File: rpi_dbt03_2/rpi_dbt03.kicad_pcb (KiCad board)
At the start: 2 copper layers, 64 x 56 mm, 33 parts, among them J2 Conn_02x03_Odd_Even, Q1 BC546, U1 ATmega8L-8PU, U2 SFH617A-1, U3 SFH617A-1, U4 SFH617A-1, Y1 8MHz

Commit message: Found a hardware Bug. Pin 18 of the ATMega8 needs to connected to Pin 24 of the Raspberry PI. This will mean that a new layout is needed, however so far you can patch it by adding one bodge wire.
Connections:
- RP1 pad 24: Net-(RP1-Pad24) -> /SPI_CS
- U1 pad 16: Net-(U1-Pad16) -> /SPI_CS
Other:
- board text added: "Warning one unconnected wire in this revision!"

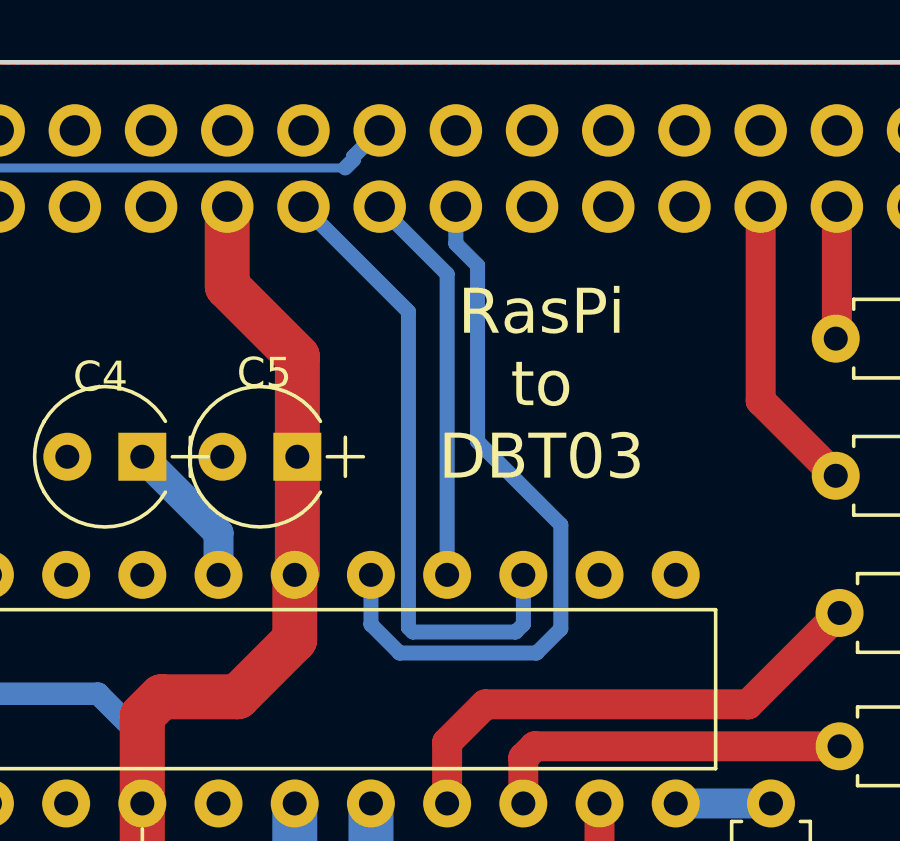
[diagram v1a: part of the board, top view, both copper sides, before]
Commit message: Added SPI_CE line and swapped incorrectly named _SD0 and _S0 netw
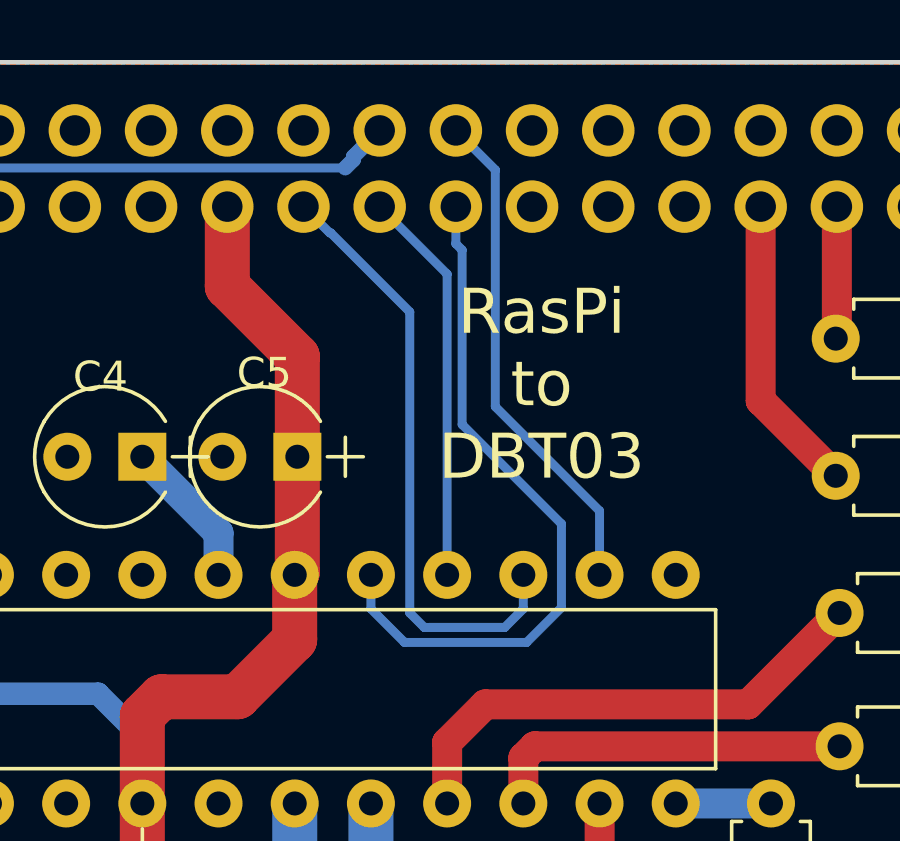
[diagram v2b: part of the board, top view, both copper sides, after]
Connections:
- R3 pad 2: /_S0 -> /_SD0
- R4 pad 2: /_SD0 -> /_S0
- U1 pad 2: /_SD0 -> /_S0
- U1 pad 3: /_S0 -> /_SD0
- U2 pad 4: /_SD0 -> /_S0
- U3 pad 4: /_S0 -> /_SD0
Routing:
- net /SPI_CS: track 0.00 -> 16.8 mm
- net /_SD0: track 33.2 -> 25.8 mm
- net /_S0: track 25.8 -> 33.2 mm
- net /MOSI: track 21.1 -> 22.9 mm
- net /SCK: track 24.2 -> 23.3 mm
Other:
- board text removed: "Warning one unconnected wire in this revision!"

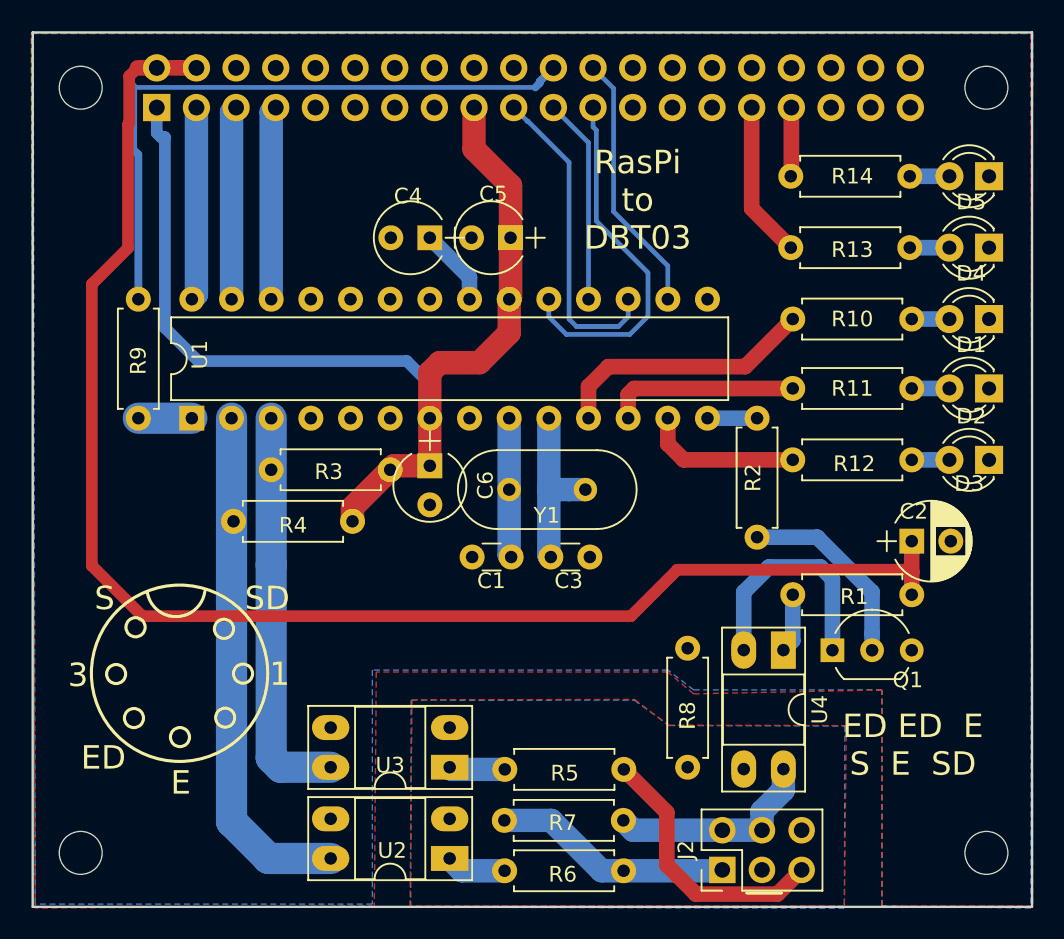
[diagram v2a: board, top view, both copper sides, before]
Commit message: Minor change, I think 2 network names have been swapped
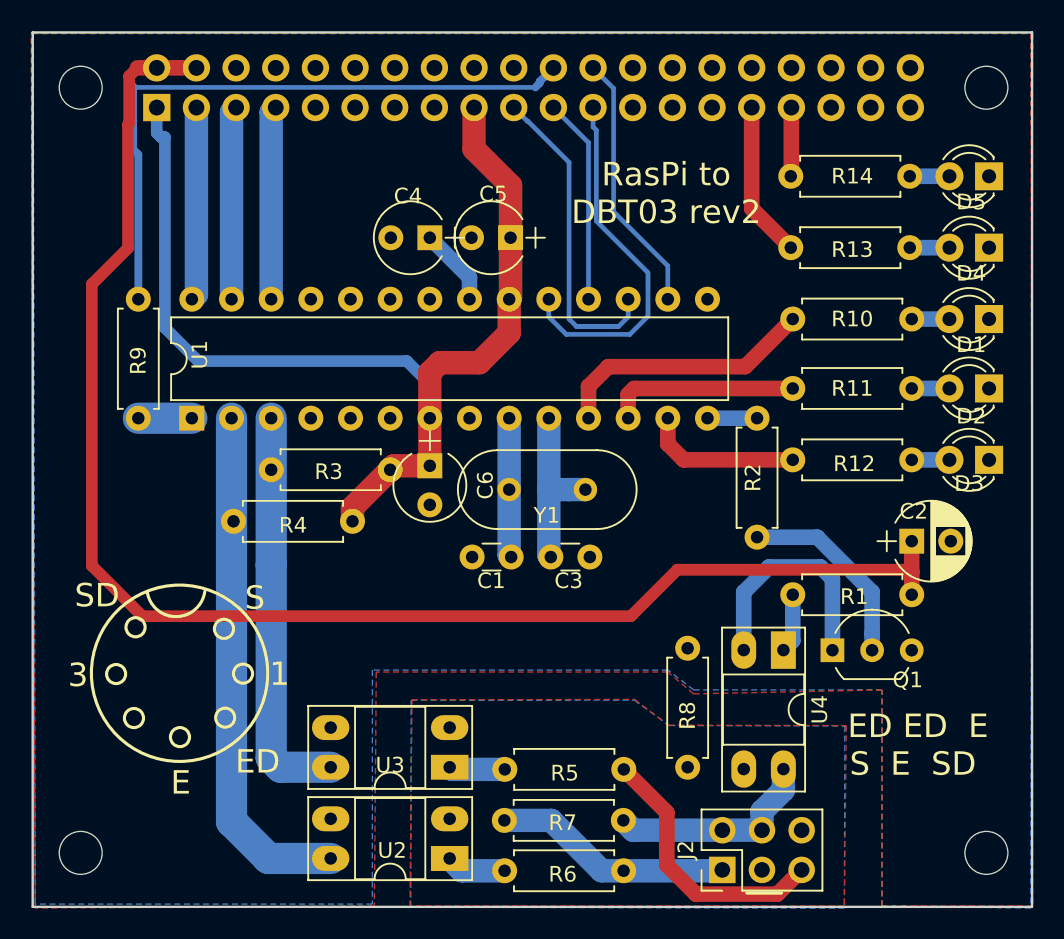
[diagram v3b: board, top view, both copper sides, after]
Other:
- board text added: "RasPi to DBT03 rev2"
- board text removed: "RasPi to DBT03"
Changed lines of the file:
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@@
   )
   (setup
-    (last_trace_width 0.3)
+    (last_trace_width 0.25)
     (user_trace_width 0.2)
     (user_trace_width 0.3)
@@
   (gr_circle (center 123.9012 117.9322) (end 124.5108 117.9068) (layer F.SilkS) (width 0.2))
   (gr_arc (start 123.6472 108.3564) (end 121.818401 108.711999) (angle -161.1962713) (layer F.SilkS) (width 0.2))
-  (gr_text SD (at 129.4892 109.0422) (layer F.SilkS)
+  (gr_text SD (at 118.5926 108.8644) (layer F.SilkS)
     (effects (font (size 1.5 1.5) (thickness 0.3)))
   )
-  (gr_text S (at 119.0752 109.0422) (layer F.SilkS)
+  (gr_text S (at 128.7018 109.0168) (layer F.SilkS)
     (effects (font (size 1.5 1.5) (thickness 0.3)))
   )
-  (gr_text ED (at 118.999 119.253) (layer F.SilkS)
+  (gr_text ED (at 128.8796 119.507) (layer F.SilkS)
     (effects (font (size 1.5 1.5) (thickness 0.3)))
   )
@@
   )
   (gr_circle (center 123.8758 113.843605) (end 128.0668 117.6274) (layer F.SilkS) (width 0.2))
-  (gr_text "ED ED  E\nS  E  SD" (at 170.8404 118.4402) (layer F.SilkS)
+  (gr_text " ED ED  E\nS  E  SD" (at 170.8404 118.4402) (layer F.SilkS)
     (effects (font (size 1.5 1.5) (thickness 0.3)))
   )
-  (gr_text "RasPi\nto\nDBT03" (at 153.2128 83.5406) (layer F.SilkS)
+  (gr_text "RasPi to\nDBT03 rev2" (at 155.0416 83.1088) (layer F.SilkS)
     (effects (font (size 1.5 1.5) (thickness 0.3)))
   )
@@
   (segment (start 170.6372 82.0166) (end 173.1772 82.0166) (width 1) (layer B.Cu) (net 57))
   (segment (start 157.6832 97.5106) (end 160.8582 97.5106) (width 1) (layer B.Cu) (net 59))
+  (segment (start 127.2032 97.5106) (end 127.2032 109.9566) (width 2) (layer B.Cu) (net 60))
+  (segment (start 129.5658 125.7046) (end 133.5532 125.7046) (width 2) (layer B.Cu) (net 60))
+  (segment (start 127.2032 109.9566) (end 127.2032 123.342) (width 2) (layer B.Cu) (net 60))
+  (segment (start 127.2032 123.342) (end 129.5658 125.7046) (width 2) (layer B.Cu) (net 60))
   (segment (start 129.7432 97.5106) (end 129.7432 106.9086) (width 2) (layer B.Cu) (net 61))
   (segment (start 130.3532 119.8626) (end 133.5532 119.8626) (width 2) (layer B.Cu) (net 61))
   (segment (start 129.7432 119.2526) (end 130.3532 119.8626) (width 2) (layer B.Cu) (net 61))
   (segment (start 129.7432 106.9086) (end 129.7432 119.2526) (width 2) (layer B.Cu) (net 61))
-  (segment (start 127.2032 97.5106) (end 127.2032 109.9566) (width 2) (layer B.Cu) (net 60))
-  (segment (start 129.5658 125.7046) (end 133.5532 125.7046) (width 2) (layer B.Cu) (net 60))
-  (segment (start 127.2032 109.9566) (end 127.2032 123.342) (width 2) (layer B.Cu) (net 60))
-  (segment (start 127.2032 123.342) (end 129.5658 125.7046) (width 2) (layer B.Cu) (net 60))
   (segment (start 151.6698 76.391) (end 151.6698 84.2836) (width 0.3) (layer B.Cu) (net 62))
   (segment (start 150.354801 75.076001) (end 151.6698 76.391) (width 0.3) (layer B.Cu) (net 62))

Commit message: Version 3 which adds 3 buttons and some configuration jumpers
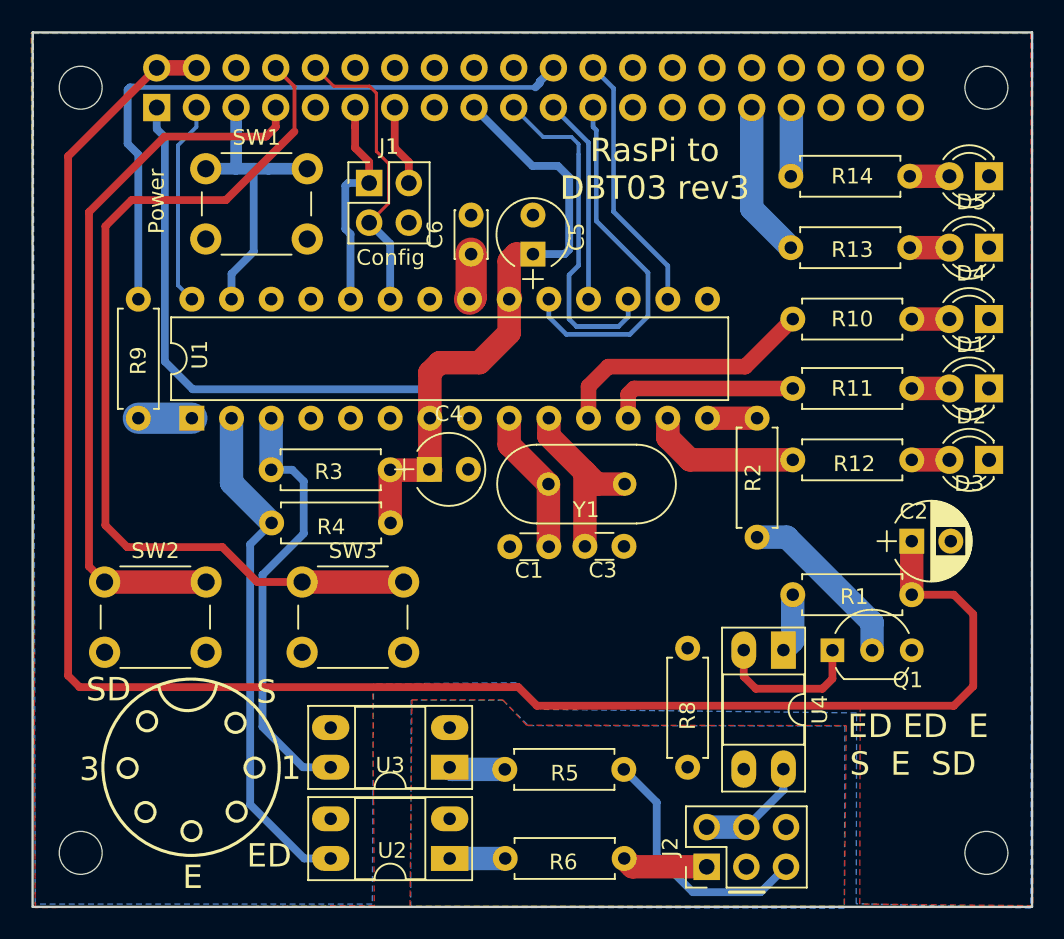
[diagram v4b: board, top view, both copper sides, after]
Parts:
- removed R7: 2k2, Resistors_ThroughHole:R_Axial_DIN0207_L6.3mm_D2.5mm_P7.62mm_Horizontal
- added J1: Conn_02x02_Counter_Clockwise, Pin_Headers:Pin_Header_Straight_2x02_Pitch2.54mm, F.Cu at (136.0, 82.4)
- added SW1: SW_Push, Buttons_Switches_ThroughHole:SW_PUSH_6mm, F.Cu at (125.6, 81.5)
- added SW2: SW_Push, Buttons_Switches_ThroughHole:SW_PUSH_6mm, F.Cu at (119.1, 108.0)
- added SW3: SW_Push, Buttons_Switches_ThroughHole:SW_PUSH_6mm, F.Cu at (131.7, 108.0)
- C6: footprint Capacitors_ThroughHole:CP_Radial_Tantal_D4.5mm_P2.50mm -> Capacitors_ThroughHole:C_Disc_D3.0mm_W2.0mm_P2.50mm
- R10, R11, R12: value 470 -> 2k2
- moved C4 14.8 mm to (139.9, 100.8), turned to 0 degrees
- moved C6 13.8 mm to (142.5, 87.0), turned to 90 degrees
- moved Y1 2.54 mm to (147.5, 101.7)
- moved C1 2.50 mm to (147.5, 105.7)
- moved R4 2.44 mm to (137.4, 104.2)
- moved C3 2.29 mm to (149.8, 105.7)
- moved C5 1.78 mm to (146.5, 87.0), turned to 90 degrees
- moved J2 1.02 mm to (157.6, 126.2)
- moved R6 0.79 mm to (152.3, 125.7)
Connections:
- C4 pad 1: Net-(C4-Pad1) -> +3V3
- C6 pad 1: +3V3 -> Net-(C6-Pad1)
- RP1 pad 10: Net-(RP1-Pad10) -> /GPIO15
- RP1 pad 11: Net-(RP1-Pad11) -> /GPIO17
- RP1 pad 12: Net-(RP1-Pad12) -> (no net)
- RP1 pad 15: Net-(RP1-Pad15) -> (no net)
- RP1 pad 16: Net-(RP1-Pad16) -> (no net)
- RP1 pad 18: Net-(RP1-Pad18) -> (no net)
- RP1 pad 26: Net-(RP1-Pad26) -> (no net)
- RP1 pad 27: Net-(RP1-Pad27) -> (no net)
- RP1 pad 28: Net-(RP1-Pad28) -> (no net)
- RP1 pad 29: /COM_A -> (no net)
- RP1 pad 32: Net-(RP1-Pad32) -> (no net)
- RP1 pad 35: Net-(RP1-Pad35) -> (no net)
- RP1 pad 36: Net-(RP1-Pad36) -> (no net)
- RP1 pad 37: /LED_RED -> (no net)
- RP1 pad 38: Net-(RP1-Pad38) -> (no net)
- RP1 pad 40: Net-(RP1-Pad40) -> (no net)
- RP1 pad 8: Net-(RP1-Pad8) -> /GPIO14
- U1 pad 15: Net-(U1-Pad15) -> (no net)
- U1 pad 21: Net-(C4-Pad1) -> Net-(C6-Pad1)
- U1 pad 23: Net-(U1-Pad23) -> /GPIO15
- U1 pad 24: Net-(U1-Pad24) -> /GPIO17
- U1 pad 25: Net-(U1-Pad25) -> (no net)
- U1 pad 26: /GPIO4 -> (no net)
- U1 pad 4: Net-(U1-Pad4) -> (no net)
- U1 pad 5: Net-(U1-Pad5) -> (no net)
- U1 pad 6: Net-(U1-Pad6) -> (no net)
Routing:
- net /GPIO14: track 0.00 -> 58.9 mm
- net /GPIO4: track 12.4 -> 46.1 mm
- net +5V: track 95.4 -> 115.6 mm
- net /GPIO15: track 0.00 -> 19.2 mm
- net /GPIO17: track 0.00 -> 14.2 mm
- net /S0: track 15.3 -> 5.50 mm
- net /GPIO3: track 12.4 -> 19.8 mm
- net /ED0: track 13.6 -> 7.24 mm
- net +3V3: track 69.7 -> 75.5 mm
- net Net-(J1-Pad2): track 0.00 -> 5.21 mm
- net Net-(Q1-Pad1): track 14.9 -> 9.79 mm
- net Net-(C4-Pad1): track 4.99 -> 0.00 mm
- net Net-(C6-Pad1): track 0.00 -> 2.99 mm
- net /_SD0: track 25.8 -> 27.9 mm
- net /MOSI: track 22.9 -> 24.5 mm
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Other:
- board text added: "Config"
- board text added: "Power"
- board text added: "RasPi to DBT03 rev3"
- board text removed: "RasPi to DBT03 rev2"
